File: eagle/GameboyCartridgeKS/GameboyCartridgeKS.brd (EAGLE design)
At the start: 49.3 x 48 mm, 1 part

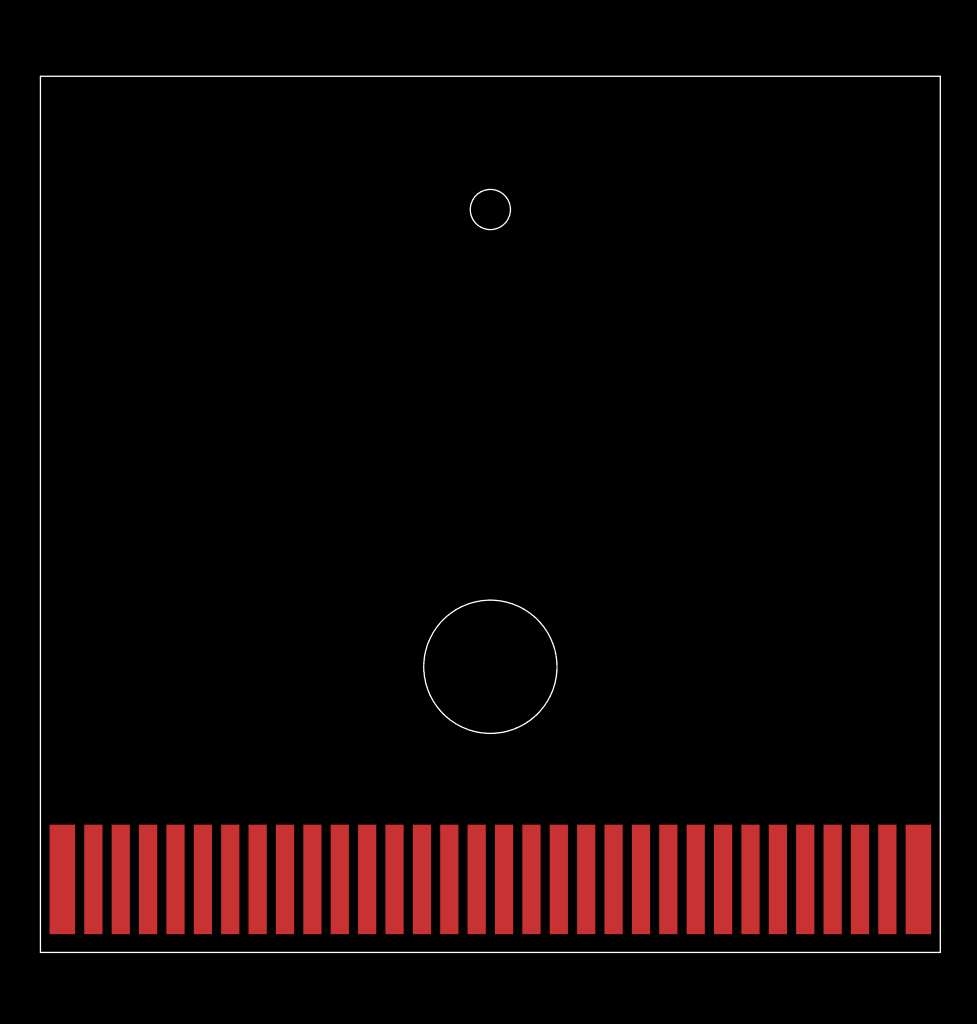
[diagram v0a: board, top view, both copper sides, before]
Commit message: Before wiring the address bus. Replaced chip by ATmega64a.
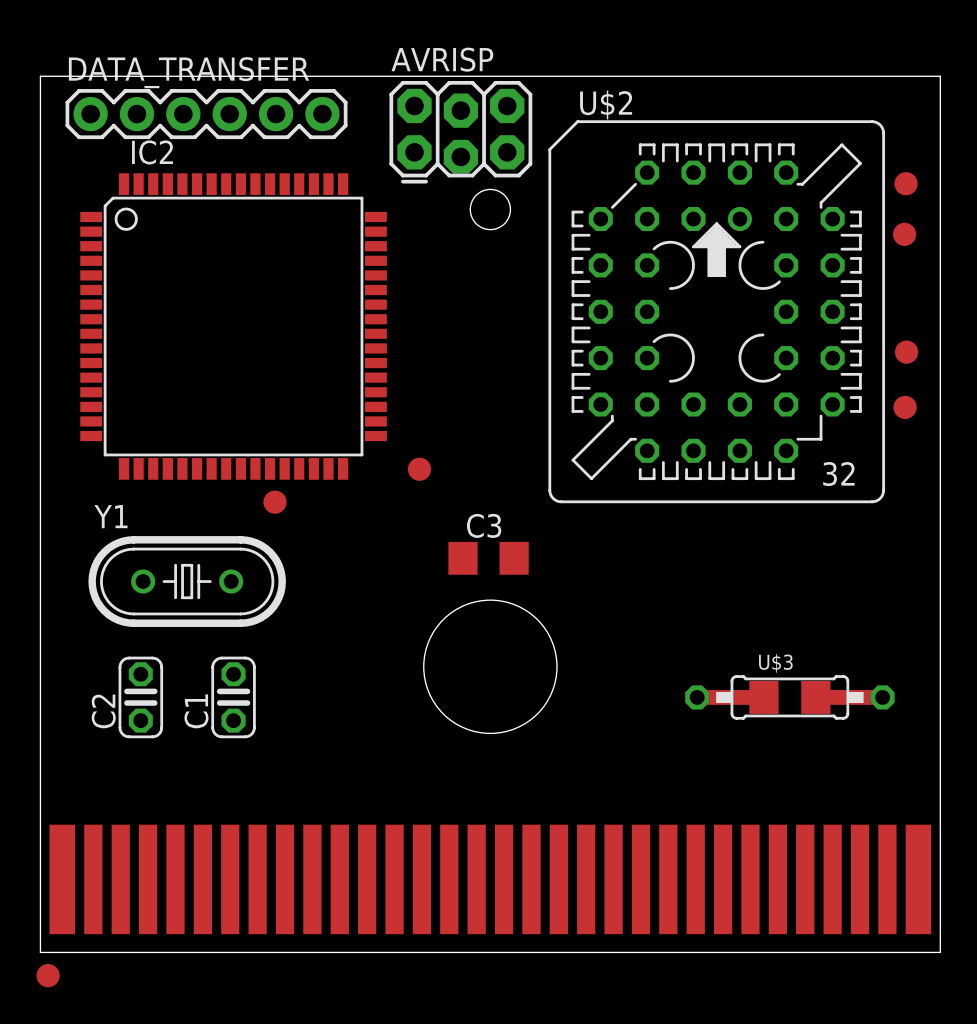
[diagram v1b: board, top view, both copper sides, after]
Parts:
- added AVRISP: AVR_SPI_PRG_62X3_LOCK, SparkFun-Connectors:2X3_LOCK
- added C1, C2: 22pF, resistor:C025-024X044
- added C3: 10uF, resistor:C1206
- added DATA_TRANSFER: (no value), SparkFun-Connectors:1X06
- added IC2: MEGA64-A, atmel:TQFP64
- added PEN, TP1, TP2, TP3, TP4, TP5, TP6: TEST-POINT3X5, SparkFun-Passives:PAD.03X.05
- added U$2: EN29F002T, kalshagar:PLCC-S32
- added U$3: RESISTOR_COMBO1206, kalshagar:207-10_SMD_COMBO
- added Y1: 16MHz max, SparkFun-FreqCtrl:HC49U-V
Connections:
- removed net 21: U$1.21
- removed net 31: U$1.31
- removed net 4: U$1.4
- new net !CE: TP1.P$1, U$1.21, U$2.22
- new net !OE: TP2.P$1, U$1.4, U$2.24
- new net !RESET: TP4.P$1, U$2.1
- new net !WE: TP3.P$1, U$1.31, U$2.31, U$3.1, U$3.4
- new net CTS: DATA_TRANSFER.2
- new net DTR: DATA_TRANSFER.6
- new net MISO_TX: AVRISP.1, DATA_TRANSFER.5, IC2.3
- new net MOSI_RX: AVRISP.4, DATA_TRANSFER.4, IC2.2
- new net N$2: C1.2, IC2.23, Y1.2
- new net N$3: AVRISP.5, IC2.20
- new net N$4: C2.2, IC2.24, Y1.1
- new net PEN: IC2.1, PEN.P$1
- new net SCK: AVRISP.3, IC2.11
- new net VCC: AVRISP.2, C3.1, DATA_TRANSFER.3, IC2.21, IC2.52, IC2.62, IC2.64, TP5.P$1, U$2.32, U$3.2, U$3.3
- net 22: now also IC2.51, U$2.13
- net 23: now also IC2.50, U$2.14
- net 24: now also IC2.49, U$2.15
- net 25: now also IC2.48, U$2.17
- net 26: now also IC2.47, U$2.18
- net 27: now also IC2.46, U$2.19
- net 28: now also IC2.45, U$2.20
- net 29: now also IC2.44, U$2.21
- net GND: now also AVRISP.6, C1.1, C2.1, C3.2, DATA_TRANSFER.1, IC2.22, IC2.53, IC2.63, TP6.P$1, U$2.16

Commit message: Stopped in the middle of wiring, will first make a modest version with simply a eeprom programmer.
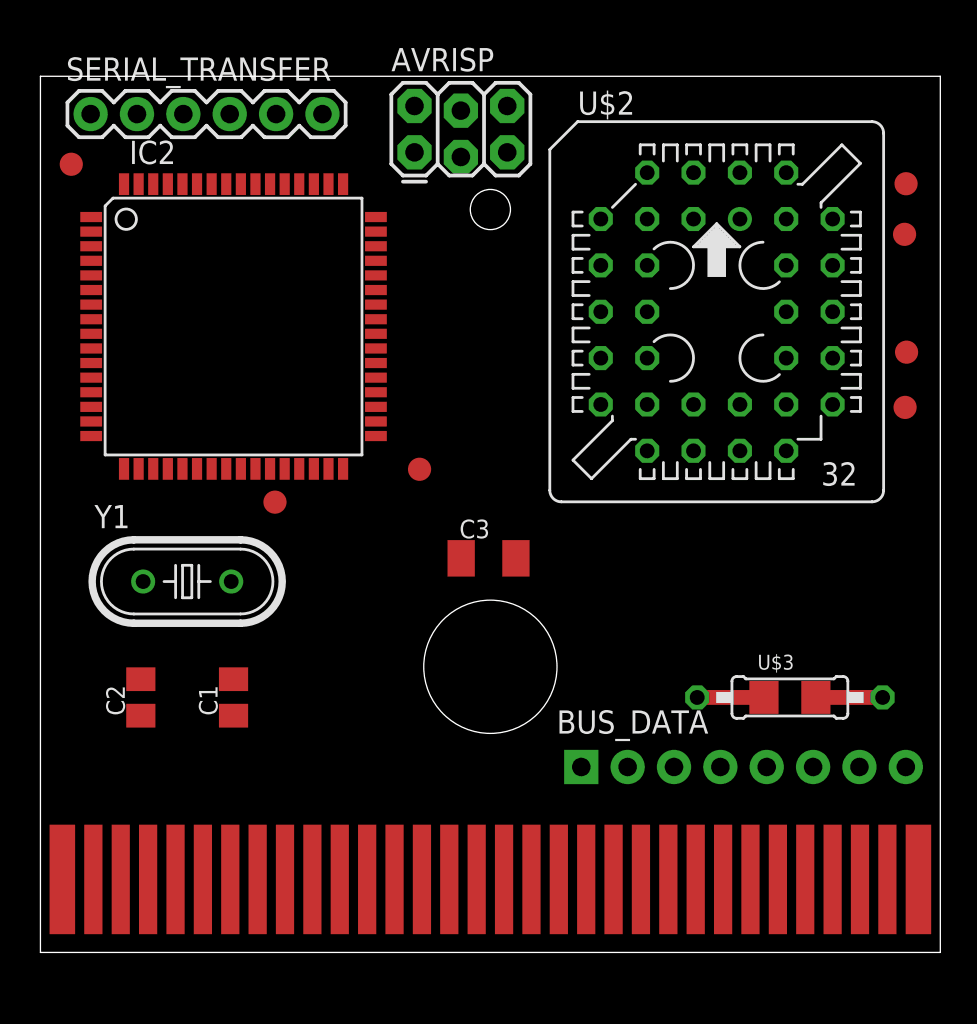
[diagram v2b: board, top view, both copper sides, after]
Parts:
- added BUS_DATA: (no value), SparkFun-Connectors:1X08_PIN1_NO_SILK
- C1, C2: device resistor:C025-024X044 -> resistor:C0805K
- C3: device resistor:C1206 -> resistor:C1206K
- moved PEN 44.5 mm to (2.54, 43.2)
- renumbered DATA_TRANSFER to SERIAL_TRANSFER
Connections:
- net 22: now also BUS_DATA.1
- net 23: now also BUS_DATA.2
- net 24: now also BUS_DATA.3
- net 25: now also BUS_DATA.4
- net 26: now also BUS_DATA.5
- net 27: now also BUS_DATA.6
- net 28: now also BUS_DATA.7
- net 29: now also BUS_DATA.8
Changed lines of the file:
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@@
 <element name="U$2" library="kalshagar" package="PLCC-S32" value="EN29F002T" x="37.9" y="35.1"/>
 <element name="AVRISP" library="SparkFun-Connectors" package="2X3_LOCK" value="AVR_SPI_PRG_62X3_LOCK" x="21.3435" y="43.832"/>
-<element name="DATA_TRANSFER" library="SparkFun-Connectors" package="1X06" value="" x="3.6" y="45.93">
+<element name="SERIAL_TRANSFER" library="SparkFun-Connectors" package="1X06" value="" x="3.6" y="45.93">
 <attribute name="PROD_ID" value="CONN-08437" x="3.6" y="45.93" size="1.778" layer="27" display="off"/>
 </element>
@@
 <element name="TP6" library="SparkFun-Passives" package="PAD.03X.05" value="TEST-POINT3X5" x="13.7" y="24.67"/>
 <element name="Y1" library="SparkFun-FreqCtrl" package="HC49U-V" value="16MHz max" x="8.89" y="20.32"/>
-<element name="C1" library="resistor" package="C025-024X044" value="22pF" x="11.43" y="13.97" rot="R90"/>
-<element name="C2" library="resistor" package="C025-024X044" value="22pF" x="6.35" y="13.97" rot="R90"/>
+<element name="C1" library="resistor" package="C0805K" value="22pF" x="11.43" y="13.97" rot="R90"/>
+<element name="C2" library="resistor" package="C0805K" value="22pF" x="6.35" y="13.97" rot="R90"/>
 <element name="U$3" library="kalshagar" package="207-10_SMD_COMBO" value="RESISTOR_COMBO1206" x="41.91" y="13.97"/>
 <element name="IC2" library="atmel" package="TQFP64" value="MEGA64-A" x="11.43" y="34.29">
@@
 <attribute name="OC_FARNELL" value="9171355" x="-6.35" y="54.61" size="1.778" layer="27" display="off"/>
 </element>
-<element name="PEN" library="SparkFun-Passives" package="PAD.03X.05" value="TEST-POINT3X5" x="1.27" y="-1.27"/>
-<element name="C3" library="resistor" package="C1206" value="10uF" x="25.4" y="21.59"/>
+<element name="PEN" library="SparkFun-Passives" package="PAD.03X.05" value="TEST-POINT3X5" x="2.54" y="43.18"/>
+<element name="C3" library="resistor" package="C1206K" value="10uF" x="25.4" y="21.59"/>
+<element name="BUS_DATA" library="SparkFun-Connectors" package="1X08_PIN1_NO_SILK" value="" x="30.48" y="10.16"/>
 </elements>
 <signals>
@@
 <contactref element="IC2" pad="53"/>
 <contactref element="IC2" pad="22"/>
-<contactref element="DATA_TRANSFER" pad="1"/>
+<contactref element="SERIAL_TRANSFER" pad="1"/>
 <contactref element="C3" pad="2"/>
 <wire x1="14.23" y1="42.09" x2="26.4235" y2="46.372" width="0" layer="19" extent="1-1"/>
@@
 <wire x1="9.43" y1="26.49" x2="6.23" y2="42.09" width="0" layer="19" extent="1-1"/>
 <wire x1="13.7" y1="24.67" x2="9.43" y2="26.49" width="0" layer="19" extent="1-1"/>
-<wire x1="11.43" y1="12.7" x2="13.7" y2="24.67" width="0" layer="19" extent="1-1"/>
-<wire x1="6.35" y1="12.7" x2="11.43" y2="12.7" width="0" layer="19" extent="1-1"/>
-<wire x1="26.8" y1="21.59" x2="13.7" y2="24.67" width="0" layer="19" extent="1-1"/>
-<wire x1="36.63" y1="27.48" x2="26.8" y2="21.59" width="0" layer="19" extent="1-1"/>
+<wire x1="11.43" y1="12.97" x2="13.7" y2="24.67" width="0" layer="19" extent="1-1"/>
+<wire x1="6.35" y1="12.97" x2="11.43" y2="12.97" width="0" layer="19" extent="1-1"/>
+<wire x1="26.9" y1="21.59" x2="13.7" y2="24.67" width="0" layer="19" extent="1-1"/>
+<wire x1="36.63" y1="27.48" x2="26.9" y2="21.59" width="0" layer="19" extent="1-1"/>
 <wire x1="48.95" y1="4" x2="36.63" y2="27.48" width="0" layer="19" extent="1-1"/>
 </signal>
@@
 <contactref element="U$2" pad="13"/>
 <contactref element="IC2" pad="51"/>
+<contactref element="BUS_DATA" pad="1"/>
 <wire x1="15.83" y1="42.09" x2="31.55" y2="30.02" width="0" layer="19" extent="1-1"/>
 <wire x1="33.7" y1="4" x2="31.55" y2="30.02" width="0" layer="19" extent="1-1"/>
+<wire x1="30.48" y1="10.16" x2="33.7" y2="4" width="0" layer="19" extent="1-1"/>
 </signal>
 <signal name="23">
@@
 <contactref element="U$2" pad="14"/>
 <contactref element="IC2" pad="50"/>
+<contactref element="BUS_DATA" pad="2"/>
 <wire x1="16.63" y1="42.09" x2="34.09" y2="27.48" width="0" layer="19" extent="1-1"/>
 <wire x1="35.25" y1="4" x2="34.09" y2="27.48" width="0" layer="19" extent="1-1"/>
+<wire x1="33.02" y1="10.16" x2="35.25" y2="4" width="0" layer="19" extent="1-1"/>
 </signal>
 <signal name="24">
@@
 <contactref element="U$2" pad="15"/>
 <contactref element="IC2" pad="49"/>
+<contactref element="BUS_DATA" pad="3"/>
 <wire x1="17.43" y1="42.09" x2="34.09" y2="30.02" width="0" layer="19" extent="1-1"/>
 <wire x1="36.75" y1="4" x2="34.09" y2="30.02" width="0" layer="19" extent="1-1"/>
+<wire x1="35.56" y1="10.16" x2="36.75" y2="4" width="0" layer="19" extent="1-1"/>
 </signal>
 <signal name="25">
@@
 <contactref element="U$2" pad="17"/>
 <contactref element="IC2" pad="48"/>
+<contactref element="BUS_DATA" pad="4"/>
 <wire x1="19.23" y1="40.29" x2="36.63" y2="30.02" width="0" layer="19" extent="1-1"/>
 <wire x1="38.25" y1="4" x2="36.63" y2="30.02" width="0" layer="19" extent="1-1"/>
+<wire x1="38.1" y1="10.16" x2="38.25" y2="4" width="0" layer="19" extent="1-1"/>
 </signal>
 <signal name="26">
@@
 <contactref element="U$2" pad="18"/>
 <contactref element="IC2" pad="47"/>
+<contactref element="BUS_DATA" pad="5"/>
 <wire x1="19.23" y1="39.49" x2="39.17" y2="27.48" width="0" layer="19" extent="1-1"/>
 <wire x1="39.75" y1="4" x2="39.17" y2="27.48" width="0" layer="19" extent="1-1"/>
+<wire x1="40.64" y1="10.16" x2="39.75" y2="4" width="0" layer="19" extent="1-1"/>
 </signal>
 <signal name="30">
@@
 <contactref element="U$2" pad="19"/>
 <contactref element="IC2" pad="46"/>
+<contactref element="BUS_DATA" pad="6"/>
 <wire x1="19.23" y1="38.69" x2="39.17" y2="30.02" width="0" layer="19" extent="1-1"/>
 <wire x1="41.25" y1="4" x2="39.17" y2="30.02" width="0" layer="19" extent="1-1"/>
+<wire x1="43.18" y1="10.16" x2="41.25" y2="4" width="0" layer="19" extent="1-1"/>
 </signal>
 <signal name="28">
@@
 <contactref element="U$2" pad="20"/>
 <contactref element="IC2" pad="45"/>
+<contactref element="BUS_DATA" pad="7"/>
 <wire x1="42.75" y1="4" x2="41.71" y2="27.48" width="0" layer="19" extent="1-1"/>
 <wire x1="19.23" y1="37.89" x2="41.71" y2="27.48" width="0" layer="19" extent="1-1"/>
+<wire x1="45.72" y1="10.16" x2="42.75" y2="4" width="0" layer="19" extent="1-1"/>
 </signal>
 <signal name="29">
@@
 <contactref element="U$2" pad="21"/>
 <contactref element="IC2" pad="44"/>
+<contactref element="BUS_DATA" pad="8"/>
 <wire x1="19.23" y1="37.09" x2="44.25" y2="30.02" width="0" layer="19" extent="1-1"/>
 <wire x1="44.25" y1="4" x2="44.25" y2="30.02" width="0" layer="19" extent="1-1"/>
+<wire x1="48.26" y1="10.16" x2="44.2" y2="4" width="0" layer="19" extent="1-1"/>
 </signal>
 <signal name="VCC">
@@
 <contactref element="IC2" pad="21"/>
 <contactref element="IC2" pad="52"/>
-<contactref element="DATA_TRANSFER" pad="3"/>
+<contactref element="SERIAL_TRANSFER" pad="3"/>
 <contactref element="C3" pad="1"/>
 <wire x1="21.3435" y1="46.372" x2="39.17" y2="42.72" width="0" layer="19" extent="1-1"/>
@@
 <wire x1="8.63" y1="26.49" x2="7.03" y2="42.09" width="0" layer="19" extent="1-1"/>
 <wire x1="21.62" y1="26.47" x2="8.63" y2="26.49" width="0" layer="19" extent="1-1"/>
-<wire x1="24" y1="21.59" x2="21.62" y2="26.47" width="0" layer="19" extent="1-1"/>
-<wire x1="43.18" y1="13.97" x2="24" y2="21.59" width="0" layer="19" extent="1-1"/>
+<wire x1="23.9" y1="21.59" x2="21.62" y2="26.47" width="0" layer="19" extent="1-1"/>
+<wire x1="43.18" y1="13.97" x2="23.9" y2="21.59" width="0" layer="19" extent="1-1"/>
 <wire x1="43.332" y1="13.97" x2="43.18" y2="13.97" width="0" layer="19" extent="1-1"/>
 </signal>
@@
 <contactref element="AVRISP" pad="1"/>
 <contactref element="IC2" pad="3"/>
-<contactref element="DATA_TRANSFER" pad="5"/>
+<contactref element="SERIAL_TRANSFER" pad="5"/>
 <wire x1="13.76" y1="45.93" x2="21.3435" y2="43.832" width="0" layer="19" extent="1-1"/>
 <wire x1="3.63" y1="38.69" x2="13.76" y2="45.93" width="0" layer="19" extent="1-1"/>
@@
 <contactref element="AVRISP" pad="4"/>
 <contactref element="IC2" pad="2"/>
-<contactref element="DATA_TRANSFER" pad="4"/>
+<contactref element="SERIAL_TRANSFER" pad="4"/>
 <wire x1="11.22" y1="45.93" x2="23.8835" y2="46.118" width="0" layer="19" extent="1-1"/>
 <wire x1="3.63" y1="39.49" x2="11.22" y2="45.93" width="0" layer="19" extent="1-1"/>
@@
 <contactref element="IC2" pad="23"/>
 <wire x1="11.303" y1="20.32" x2="10.23" y2="26.49" width="0" layer="19" extent="1-1"/>
-<wire x1="11.43" y1="15.24" x2="11.303" y2="20.32" width="0" layer="19" extent="1-1"/>
+<wire x1="11.43" y1="14.97" x2="11.303" y2="20.32" width="0" layer="19" extent="1-1"/>
 </signal>
 <signal name="N$4">
@@
 <contactref element="IC2" pad="24"/>
 <wire x1="6.477" y1="20.32" x2="11.03" y2="26.49" width="0" layer="19" extent="1-1"/>
-<wire x1="6.35" y1="15.24" x2="6.477" y2="20.32" width="0" layer="19" extent="1-1"/>
+<wire x1="6.35" y1="14.97" x2="6.477" y2="20.32" width="0" layer="19" extent="1-1"/>
 </signal>
 <signal name="PEN">
 <contactref element="PEN" pad="P$1"/>
 <contactref element="IC2" pad="1"/>
-<wire x1="1.27" y1="-1.27" x2="3.63" y2="40.29" width="0" layer="19" extent="1-1"/>
+<wire x1="3.63" y1="40.29" x2="2.54" y2="43.18" width="0" layer="19" extent="1-1"/>
 </signal>
 <signal name="CTS">
-<contactref element="DATA_TRANSFER" pad="2"/>
+<contactref element="SERIAL_TRANSFER" pad="2"/>
 </signal>
 <signal name="DTR">
-<contactref element="DATA_TRANSFER" pad="6"/>
+<contactref element="SERIAL_TRANSFER" pad="6"/>
 </signal>
 </signals>
